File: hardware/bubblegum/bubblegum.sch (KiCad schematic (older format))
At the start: 126 parts, among them P1 RX_OUT, P2 RX_ONLY, P3 SERIAL, P4 TX/RX, P5 CONN_2, P6 TX_IN, P7 VCC, P8 SWITCH_CTRL, Q1 MOSFET_P, Q2 MOSFET_N, Q3 MOSFET_P, Q4 MOSFET_N, T1 RX_IF_BALUN, T2 RX_HIGHPASS_BALUN, T3 RX_LOWPASS_BALUN, T4 TX_HIGHPASS_BALUN, T5 TX_LOWPASS_BALUN, T6 TX_IF_BALUN, U1 PE4140, U10 TX_HIGHPASS_FILTER, U11 PE4140, U12 SKY13350, U13 TX_LOWPASS_FILTER, U14 RF1226, U15 PE4140, U16 GSG-74HC04, U2 RF1226, U3 RX_HIGHPASS_FILTER, U4 SKY13350, U5 SKY13350, U6 PE4140, U7 RX_LOWPASS_FILTER, U8 SKY13350, U9 TRF3765

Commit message: tied unused logic input to VCC
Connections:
- wire segments 411 -> 414
- no-connect marks 8 -> 5

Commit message: Bubblegum redesign assuming TX_BALUN and RX_BALUN can operate from 10 MHz to 6 GHz
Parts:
- removed C1, C10, C11, C13, C2, C23, C24, C3, C37, C38, C4, C60, C61, C62, C64, C66, C67, C68, C69, C7: C, symbol C
- removed L1, L2, L7, L8: INDUCTOR, symbol INDUCTOR
- removed R11, R12, R4, R5: R, symbol R
- removed T3: RX_LOWPASS_BALUN, symbol BALUN-RFXF9503
- removed T5: TX_LOWPASS_BALUN, symbol BALUN-RFXF9503
- removed U1, U15: PE4140, symbol PE4140
- removed U14, U2: RF1226, symbol RF1226
- added C? (x10): C, symbol C
- added U? (x2): SKY13350, symbol SKY13350
- T2: value RX_HIGHPASS_BALUN -> RX_BALUN
- T4: value TX_HIGHPASS_BALUN -> TX_BALUN
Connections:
- wire segments 414 -> 346
- no-connect marks 5 -> 9
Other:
- note added: "switchable image reject filters"
- note removed: "DC GND connection on IF1 needed?"
- note removed: "DC GND connection on IF1, IF2 needed?"
- note removed: "DC GND connection on RF1 needed?"
- note removed: "DC GND connection on RF1, RF2 needed?"
- moved on the sheet: C12, C14, C15, C16, C17, C18, C19, C20, C21, C22, C25, C26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

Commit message: minor cleanup
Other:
- note added: "amplifier will likely\nend up here"
- note added: "balun here may not not be needed if\ndirect connection to MAX2837 is made"
- note removed: "balun here not needed if direct\nconnection to MAX2837 is made"
- moved on the sheet: C?

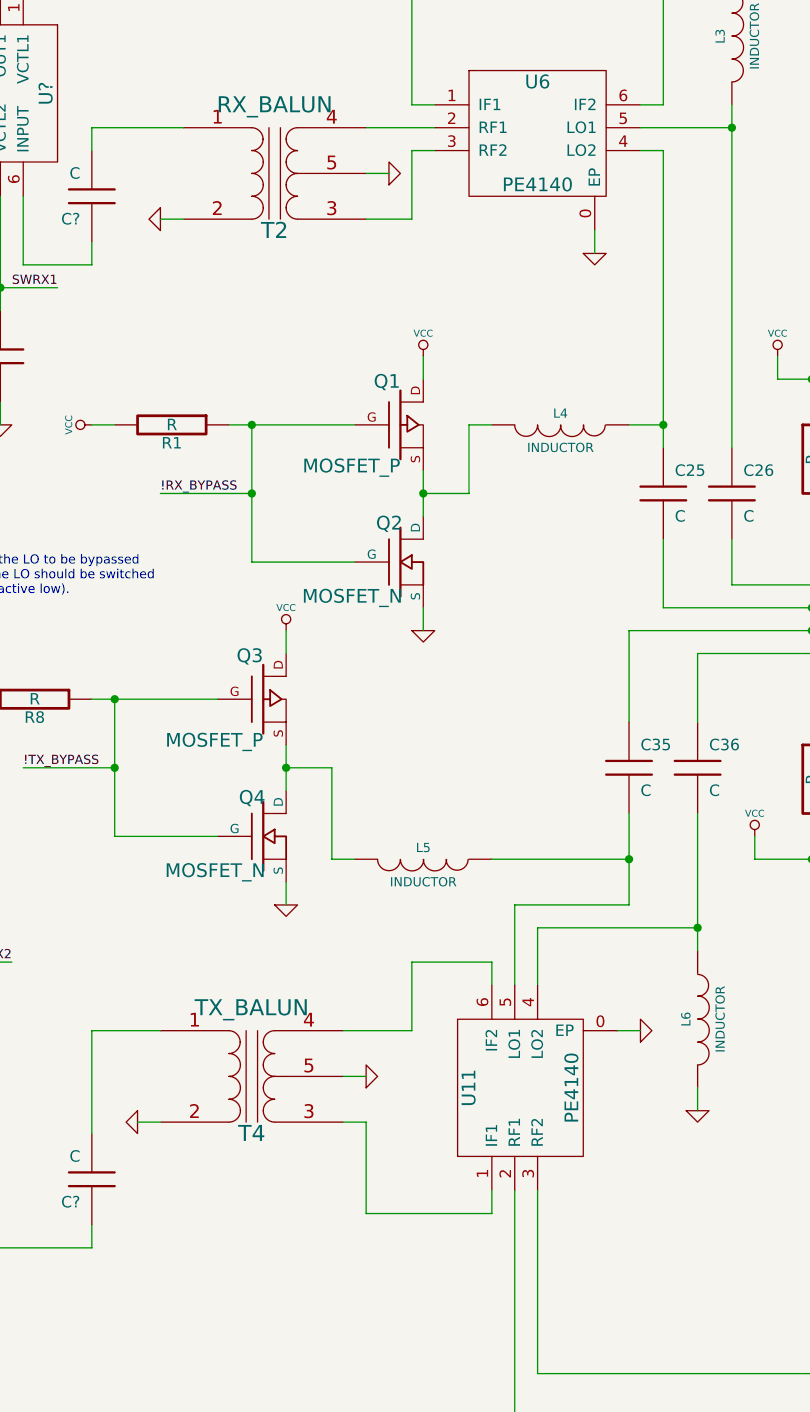
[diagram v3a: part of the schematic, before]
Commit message: disconnected pin 5 per B0310J50100AHF datasheet
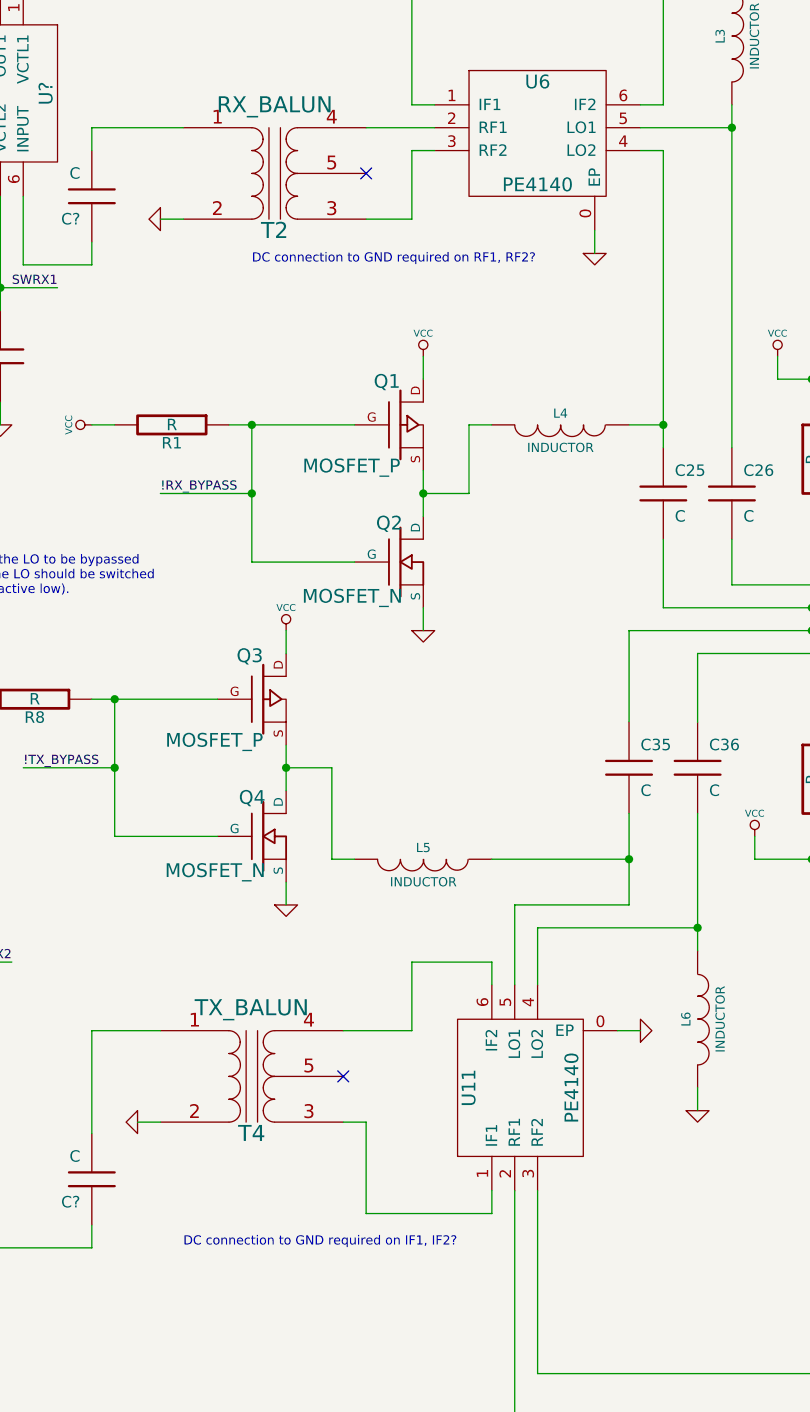
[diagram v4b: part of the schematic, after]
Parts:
- T2, T4: Description (none) -> Ultra Low Profile 0805 Balun 50 to 100 Balanced; Manufacturer (none) -> Anaren; Part Number (none) -> B0310J50100AHF
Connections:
- net GND: no longer T2.5 (PM), T4.5 (PM)
- no-connect marks 9 -> 11
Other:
- note added: "DC connection to GND required on IF1, IF2?"
- note added: "DC connection to GND required on RF1, RF2?"
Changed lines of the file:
@@
-EESchema Schematic File Version 2  date Thu Jun 21 11:46:05 2012
+EESchema Schematic File Version 2  date Thu Jun 21 12:06:12 2012
 LIBS:power
 LIBS:device
@@
 Comment4 ""
 $EndDescr
+Text Notes 7400 7750 0    40   ~ 0
+DC connection to GND required on IF1, IF2?
+Text Notes 7700 3450 0    40   ~ 0
+DC connection to GND required on RF1, RF2?
+NoConn ~ 8100 7000
+$Comp
+L BALUN T2
+U 1 1 4FE35EF4
+P 7800 3050
+F 0 "T2" H 7800 3300 70  0000 C CNN
+F 1 "RX_BALUN" H 7800 2750 70  0000 C CNN
+F 4 "Anaren" H 7800 3050 60  0001 C CNN "Manufacturer"
+F 5 "B0310J50100AHF" H 7800 3050 60  0001 C CNN "Part Number"
+F 6 "Ultra Low Profile 0805 Balun 50 to 100 Balanced" H 7800 3050 60  0001 C CNN "Description"
+	1    7800 3050
+	-1   0    0    1
+$EndComp
+NoConn ~ 8200 3050
 Text Notes 11850 1150 0    40   ~ 0
 balun here may not not be needed if\ndirect connection to MAX2837 is made
@@
 	2250 5250 2250 5150
 Wire Wire Line
-	8300 3050 8200 3050
-Wire Wire Line
 	7300 3250 7400 3250
 Wire Wire Line
@@
 Wire Wire Line
 	8750 6500 8750 6600
-Wire Wire Line
-	8200 7000 8100 7000
 Wire Wire Line
 	5250 6800 5350 6800
@@
 $EndComp
 $Comp
-L GND #PWR10
-U 1 1 4FE0E7AF
-P 8300 3050
-F 0 "#PWR10" H 8300 3050 30  0001 C CNN
-F 1 "GND" H 8300 2980 30  0001 C CNN
-	1    8300 3050
-	0    -1   -1   0
-$EndComp
-$Comp
 L GND #PWR11
 U 1 1 4FE0E7A7
@@
 $EndComp
 $Comp
-L GND #PWR59
-U 1 1 4FE0E735
-P 8200 7000
-F 0 "#PWR59" H 8200 7000 30  0001 C CNN
-F 1 "GND" H 8200 6930 30  0001 C CNN
-	1    8200 7000
-	0    -1   -1   0
-$EndComp
-$Comp
 L GSG-SMA-CONN P6
 U 1 1 4FE0DF72
@@
 $EndComp
 $Comp
-L BALUN T2
-U 1 1 4FE0D339
-P 7800 3050
-F 0 "T2" H 7800 3300 70  0000 C CNN
-F 1 "RX_BALUN" H 7800 2750 70  0000 C CNN
-	1    7800 3050
-	-1   0    0    1
-$EndComp
-$Comp
 L BALUN T4
 U 1 1 4FE0D2EC
@@
 F 0 "T4" H 7700 7250 70  0000 C CNN
 F 1 "TX_BALUN" H 7700 6700 70  0000 C CNN
+F 4 "Anaren" H 7700 7000 60  0001 C CNN "Manufacturer"
+F 5 "B0310J50100AHF" H 7700 7000 60  0001 C CNN "Part Number"
+F 6 "Ultra Low Profile 0805 Balun 50 to 100 Balanced" H 7700 7000 60  0001 C CNN "Description"
 	1    7700 7000
 	-1   0    0    1

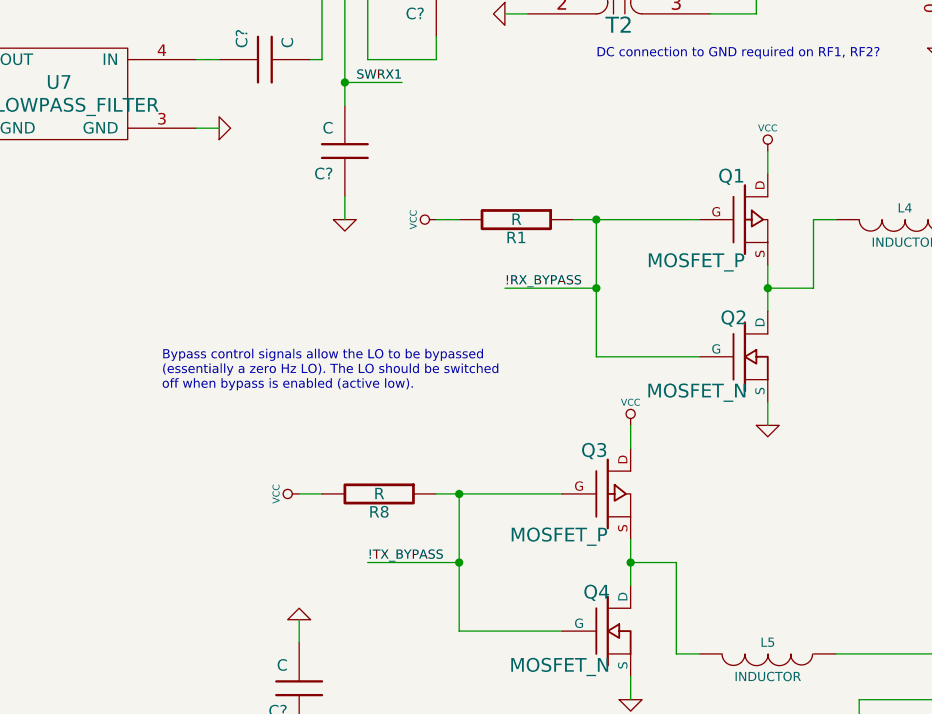
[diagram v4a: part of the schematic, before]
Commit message: fixed p-channel mosfet orientation
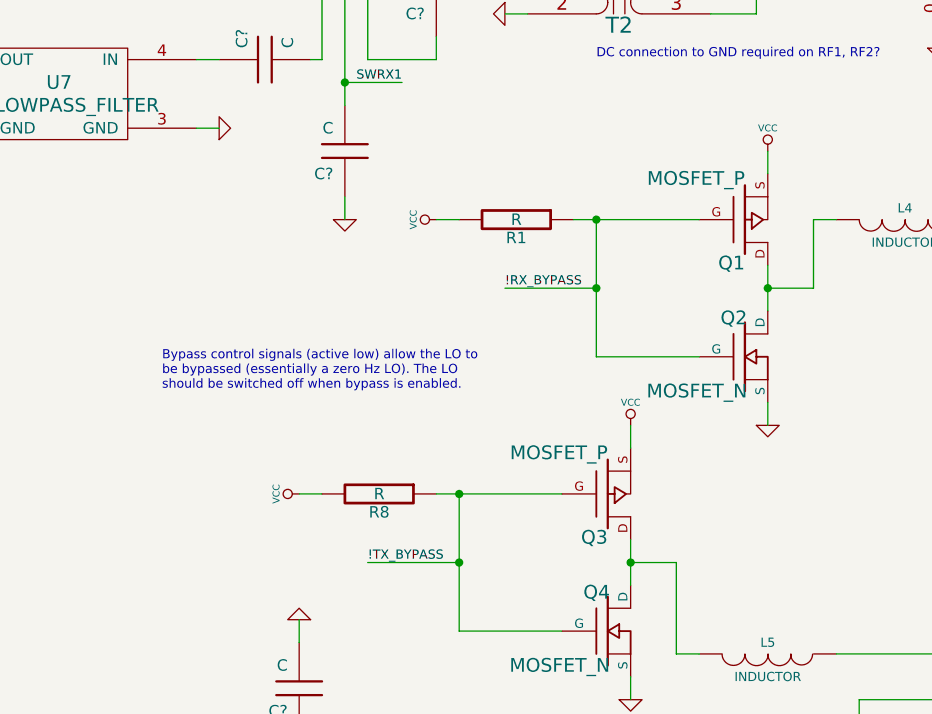
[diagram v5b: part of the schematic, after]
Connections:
- net VCC: now also Q1.S, Q3.S; no longer Q1.D, Q3.D
- net at L4.2, Q2.D: now also Q1.D; no longer Q1.S
- net at L5.2, Q4.D: now also Q3.D; no longer Q3.S
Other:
- note added: "Bypass control signals (active low) allow the LO to\nbe bypassed (essentially a zero Hz LO). The LO\nshould be switched off when bypass is enabled."
- note removed: "Bypass control signals allow the LO to be bypassed\n(essentially a zero Hz LO). The LO should be switched\noff when bypass is enabled (active low)."
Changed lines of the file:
@@
-EESchema Schematic File Version 2  date Thu Jun 21 12:06:12 2012
+EESchema Schematic File Version 2  date Wed Jun 27 21:51:49 2012
 LIBS:power
 LIBS:device
@@
 Sheet 1 1
 Title ""
-Date "21 jun 2012"
+Date "28 jun 2012"
 Rev ""
 Comp ""
@@
 Comment4 ""
 $EndDescr
+Wire Wire Line
+	9650 7050 9650 7150
 Text Notes 7400 7750 0    40   ~ 0
 DC connection to GND required on IF1, IF2?
@@
 Wire Wire Line
 	9800 2050 9800 2150
-Wire Wire Line
-	9650 7050 9650 7150
 Wire Wire Line
 	9800 4650 9800 4850
@@
 ferrite beads needed?
 Text Notes 5800 4900 0    40   ~ 0
-Bypass control signals allow the LO to be bypassed\n(essentially a zero Hz LO). The LO should be switched\noff when bypass is enabled (active low).
+Bypass control signals (active low) allow the LO to\nbe bypassed (essentially a zero Hz LO). The LO\nshould be switched off when bypass is enabled.
 Text Notes 11850 8000 0    40   ~ 0
 balun here may not not be needed if\ndirect connection to MAX2837 is made
@@
 F 1 "MOSFET_P" H 7750 5170 60  0000 R CNN
 	1    7750 5350
-	1    0    0    -1
+	1    0    0    1
 $EndComp
 $Comp
@@
 F 1 "MOSFET_P" H 8350 3970 60  0000 R CNN
 	1    8350 4150
-	1    0    0    -1
-$EndComp
-$Comp
+	1    0    0    1
+$EndComp
+$Comp

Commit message: matched n-channel mosfets to keep impedance the same between differential paths
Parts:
- added Q? (x2): MOSFET_N, symbol MOSFET_N
- Q2, Q4: Part Number (none) -> DMN2300UFB4
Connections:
- net GND: now also Q?.S, Q?.S; no longer L3.1, L6.2
- net VCC: now also Q?.G, Q?.G
- new net: L3.1, Q?.D
- new net: L6.2, Q?.D
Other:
- moved on the sheet: L3
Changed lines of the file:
@@
-EESchema Schematic File Version 2  date Wed Jun 27 21:51:49 2012
+EESchema Schematic File Version 2  date Wed Jun 27 21:56:30 2012
 LIBS:power
 LIBS:device
@@
 $EndDescr
 Wire Wire Line
+	10900 2550 11000 2550
+Wire Wire Line
+	11000 2550 11000 2450
+Wire Wire Line
+	10500 2250 10600 2250
+Wire Wire Line
+	10600 2250 10600 2350
+Wire Wire Line
+	10050 7250 10050 7350
+Wire Wire Line
+	10050 7350 9950 7350
+Wire Wire Line
 	9650 7050 9650 7150
-Text Notes 7400 7750 0    40   ~ 0
-DC connection to GND required on IF1, IF2?
-Text Notes 7700 3450 0    40   ~ 0
-DC connection to GND required on RF1, RF2?
-NoConn ~ 8100 7000
-$Comp
-L BALUN T2
-U 1 1 4FE35EF4
-P 7800 3050
-F 0 "T2" H 7800 3300 70  0000 C CNN
-F 1 "RX_BALUN" H 7800 2750 70  0000 C CNN
-F 4 "Anaren" H 7800 3050 60  0001 C CNN "Manufacturer"
-F 5 "B0310J50100AHF" H 7800 3050 60  0001 C CNN "Part Number"
-F 6 "Ultra Low Profile 0805 Balun 50 to 100 Balanced" H 7800 3050 60  0001 C CNN "Description"
-	1    7800 3050
-	-1   0    0    1
-$EndComp
-NoConn ~ 8200 3050
-Text Notes 11850 1150 0    40   ~ 0
-balun here may not not be needed if\ndirect connection to MAX2837 is made
-Text Notes 3450 4550 0    40   ~ 0
-amplifier will likely\nend up here
-Text Notes 2450 6900 0    40   ~ 0
-amplifier will likely\nend up here
 Wire Wire Line
 	6900 1950 6900 2050
@@
 	6300 8050 6550 8050
 Wire Wire Line
-	6300 7650 6300 8150
+	6300 8150 6300 7650
 Wire Wire Line
 	6400 5900 6400 6000
@@
 Connection ~ 7100 5350
 Wire Wire Line
-	7000 5350 7550 5350
+	7550 5350 7000 5350
 Connection ~ 7700 4150
 Wire Wire Line
-	7600 4150 8150 4150
+	8150 4150 7600 4150
 Connection ~ 1950 6250
 Wire Wire Line
@@
 Connection ~ 2650 3550
 Wire Wire Line
-	2650 3650 2650 3450
+	2650 3450 2650 3650
 Wire Wire Line
 	2850 3550 2650 3550
 Wire Wire Line
-	4150 2250 4150 1950
+	4150 1950 4150 2250
 Connection ~ 4050 3500
 Wire Wire Line
@@
 	14100 5750 14100 6050
 Wire Wire Line
-	12750 5250 13500 5250
+	13500 5250 12750 5250
 Connection ~ 14100 5250
 Wire Wire Line
@@
 Connection ~ 13400 5250
 Wire Wire Line
-	13100 5350 13100 5250
+	13100 5250 13100 5350
 Wire Wire Line
 	11450 3950 11450 4050
@@
 	7850 5050 7850 5150
 Wire Wire Line
-	9800 2050 9800 2150
-Wire Wire Line
 	9800 4650 9800 4850
 Wire Wire Line
@@
 	8150 4750 7700 4750
 Wire Wire Line
-	8450 4350 8450 4550
+	8450 4550 8450 4350
 Connection ~ 9500 4150
 Wire Wire Line
@@
 	4250 3250 4250 3150
 Wire Wire Line
-	1550 5150 1750 5150
+	1750 5150 1550 5150
 Wire Wire Line
 	1650 5850 1650 5750
@@
 Connection ~ 850  5450
 Wire Wire Line
-	1550 3450 1750 3450
+	1750 3450 1550 3450
 Wire Wire Line
 	850  4050 850  3650
@@
 	7850 6250 7850 6150
 Wire Wire Line
-	7850 5750 7850 5550
+	7850 5550 7850 5750
 Wire Wire Line
 	7100 5950 7550 5950
@@
 	9500 4950 10850 4950
 Wire Wire Line
-	9650 6450 9650 5850
+	9650 5850 9650 6450
 Connection ~ 9650 6350
 Wire Wire Line
-	9800 2750 9800 4250
+	9800 4250 9800 2250
 Connection ~ 9800 2850
 Wire Wire Line
@@
 Connection ~ 10600 6050
 Wire Wire Line
-	10300 6750 10300 6550
+	10300 6550 10300 6750
 Wire Wire Line
 	10600 6550 10600 6650
@@
 	12150 3950 12150 4050
 Wire Wire Line
-	12750 4850 15400 4850
-Wire Wire Line
-	13400 5250 13400 5350
+	15400 4850 12750 4850
+Wire Wire Line
+	13400 5350 13400 5250
 Connection ~ 13100 5250
 Wire Wire Line
-	14000 5250 14200 5250
+	14200 5250 14000 5250
 Wire Wire Line
 	14800 5350 14800 5250
@@
 	16100 4850 16100 4750
 Wire Wire Line
-	3250 8150 3250 7800
+	3250 7800 3250 8150
 Wire Wire Line
 	3150 6700 3350 6700
 Wire Wire Line
-	3350 6900 3350 6600
+	3350 6600 3350 6900
 Connection ~ 3350 6700
 Wire Wire Line
@@
 Connection ~ 6900 2050
 Wire Wire Line
-	4050 3600 4050 3150
+	4050 3150 4050 3600
 Wire Wire Line
 	4150 1450 4150 1550
@@
 	8200 7600 8750 7600
 Wire Wire Line
-	6600 3650 6600 3150
-Wire Wire Line
-	6400 6400 6400 6750
+	6600 3150 6600 3650
+Wire Wire Line
+	6400 6750 6400 6400
 Wire Wire Line
 	6650 6500 6400 6500
@@
 Wire Wire Line
 	3400 4650 3400 3150
+Wire Wire Line
+	9650 7550 9650 7650
+Wire Wire Line
+	10600 2850 10600 2750
+Wire Wire Line
+	9800 2250 9900 2250
+$Comp
+L VCC #PWR?
+U 1 1 4FEBD54F
+P 11000 2450
+F 0 "#PWR?" H 11000 2550 30  0001 C CNN
+F 1 "VCC" H 11000 2550 30  0000 C CNN
+	1    11000 2450
+	1    0    0    -1
+$EndComp
+$Comp
+L MOSFET_N Q?
+U 1 1 4FEBD52A
+P 10700 2550
+F 0 "Q?" H 10710 2720 60  0000 R CNN
+F 1 "MOSFET_N" H 10710 2400 60  0000 R CNN
+F 4 "DMN2300UFB4" H 10700 2550 60  0001 C CNN "Part Number"
+	1    10700 2550
+	-1   0    0    -1
+$EndComp
+$Comp
+L VCC #PWR?
+U 1 1 4FEBD516
+P 10050 7250
+F 0 "#PWR?" H 10050 7350 30  0001 C CNN
+F 1 "VCC" H 10050 7350 30  0000 C CNN
+	1    10050 7250
+	1    0    0    -1
+$EndComp
+$Comp
+L MOSFET_N Q?
+U 1 1 4FEBD4FB
+P 9750 7350
+F 0 "Q?" H 9760 7520 60  0000 R CNN
+F 1 "MOSFET_N" H 9760 7200 60  0000 R CNN
+F 4 "DMN2300UFB4" H 9750 7350 60  0001 C CNN "Part Number"
+	1    9750 7350
+	-1   0    0    -1
+$EndComp
+Text Notes 7400 7750 0    40   ~ 0
+DC connection to GND required on IF1, IF2?
+Text Notes 7700 3450 0    40   ~ 0
+DC connection to GND required on RF1, RF2?
+NoConn ~ 8100 7000
+$Comp
+L BALUN T2
+U 1 1 4FE35EF4
+P 7800 3050
+F 0 "T2" H 7800 3300 70  0000 C CNN
+F 1 "RX_BALUN" H 7800 2750 70  0000 C CNN
+F 4 "Anaren" H 7800 3050 60  0001 C CNN "Manufacturer"
+F 5 "B0310J50100AHF" H 7800 3050 60  0001 C CNN "Part Number"
+F 6 "Ultra Low Profile 0805 Balun 50 to 100 Balanced" H 7800 3050 60  0001 C CNN "Description"
+	1    7800 3050
+	-1   0    0    1
+$EndComp
+NoConn ~ 8200 3050
+Text Notes 11850 1150 0    40   ~ 0
+balun here may not not be needed if\ndirect connection to MAX2837 is made
+Text Notes 3450 4550 0    40   ~ 0
+amplifier will likely\nend up here
+Text Notes 2450 6900 0    40   ~ 0
+amplifier will likely\nend up here
 Text Notes 4750 2750 0    60   ~ 0
 switchable image reject filters
@@
 L GND #PWR66
 U 1 1 4FE0EFAF
-P 9650 7150
-F 0 "#PWR66" H 9650 7150 30  0001 C CNN
-F 1 "GND" H 9650 7080 30  0001 C CNN
-	1    9650 7150
+P 9650 7650
+F 0 "#PWR66" H 9650 7650 30  0001 C CNN
+F 1 "GND" H 9650 7580 30  0001 C CNN
+	1    9650 7650
 	1    0    0    -1
 $EndComp
@@
 F 0 "Q4" H 7760 6120 60  0000 R CNN
 F 1 "MOSFET_N" H 7760 5800 60  0000 R CNN
+F 4 "DMN2300UFB4" H 7750 5950 60  0001 C CNN "Part Number"
 	1    7750 5950
 	1    0    0    -1
@@
 F 0 "Q2" H 8360 4920 60  0000 R CNN
 F 1 "MOSFET_N" H 8360 4600 60  0000 R CNN
+F 4 "DMN2300UFB4" H 8350 4750 60  0001 C CNN "Part Number"
 	1    8350 4750
 	1    0    0    -1
@@
 L GND #PWR16
 U 1 1 4FE0EDCF
-P 9800 2050
-F 0 "#PWR16" H 9800 2050 30  0001 C CNN
-F 1 "GND" H 9800 1980 30  0001 C CNN
-	1    9800 2050
-	-1   0    0    1
+P 10600 2850
+F 0 "#PWR16" H 10600 2850 30  0001 C CNN
+F 1 "GND" H 10600 2780 30  0001 C CNN
+	1    10600 2850
+	1    0    0    -1
 $EndComp
 $Comp
 L INDUCTOR L3
 U 1 1 4FE0EDC7
-P 9800 2450
-F 0 "L3" V 9750 2450 40  0000 C CNN
-F 1 "INDUCTOR" V 9900 2450 40  0000 C CNN
-	1    9800 2450
-	1    0    0    -1
-$EndComp
-$Comp
+P 10200 2250
+F 0 "L3" V 10150 2250 40  0000 C CNN
+F 1 "INDUCTOR" V 10300 2250 40  0000 C CNN
+	1    10200 2250
+	0    1    1    0
+$EndComp
+$Comp

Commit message: bom info
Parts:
- D1, D2: Description (none) -> CERAMIC ESD DEV .5PF 7V SMD; Manufacturer (none) -> Murata; Part Number (none) -> LXES1UBBB1-008
- P1, P2, P4, P6: Description (none) -> CONN FEMALE EDGE MT FOR .062\" BD; Manufacturer (none) -> Linx; Part Number (none) -> CONSMA003.062
- U10, U3: Description (none) -> FILTER HIGHPASS WLAN&BLUETOOTH; Manufacturer (none) -> TDK; Part Number (none) -> DEA162400HT-8004B1
- U11, U6: Description (none) -> Ultra-High Linearity UltraCMOS Broadband Quad MOSFET Array; Manufacturer (none) -> Peregrine; Part Number (none) -> PE4140
- U12, U4, U5, U8, U? (x2): Description (none) -> 0.01-6.0 GHz GaAs SPDT Switch; Manufacturer (none) -> Skyworks; Part Number (none) -> SKY13350-385LF
- U13, U7: Description (none) -> FILTER LOW PASS 1880MHZ 0603 SMD; Manufacturer (none) -> AVX; Part Number (none) -> LP0603A1880ANTR
- U16: Description (none) -> IC HEX INVERTERS 14-QFN; Manufacturer (none) -> Texas Instruments; Part Number (none) -> SN74AHC04RGYR
- U9: Description (none) -> Integer-N/Fractional-N PLL with Integrated VCO; Manufacturer (none) -> Texas Instruments; Part Number (none) -> TRF3765

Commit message: passive values
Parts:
- added C?: 100nF, symbol C
- C12, C15, C17, C19, C22, C29, C40, C45, C48, C51, C54, C63, C9, C? (x4): value C -> 10nF
- C14, C20, C21, C30, C42, C5, C65, C8, C? (x4): value C -> 33pF
- C16, C39, C44: value C -> 27pF
- C18, C41, C46, C49, C52, C55, C57, C59: value C -> 1uF
- C25, C26, C35, C36: value C -> 220pF
- C43, C6, C? (x2): value C -> 100pF
- C47, C50, C53, C56, C58: value C -> 4.7pF
- R1, R8: value R -> 10k
- R10, R2, R3, R9: value R -> 100
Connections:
- net GND: now also C?.2
- net VCC: now also C?.1
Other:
- note added: "switch control logic ensures valid switch configurations"
- moved on the sheet: P8
